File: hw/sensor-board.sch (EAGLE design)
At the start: 51 parts, among them U1 LT1762EMS8-3.3PBF, U2 ULN2003LVPWR, U3 ULN2003LVPWR, U4 PCA9685PW, U5 AT42QT1070-SSU, X1 MOLEX-501953-0407, X2 MOLEX-501953-0407

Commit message: Switched VDD of LED PWM driver to 3.3V.
Added an LDO to generate VDD for LED PWM driver.
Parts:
- added C5: 0.01uF 25V, rcl:C-EUC0603K
- added C6, C8: 1uF 25V, rcl:C-EUC0603K
- added U6: TPS730XX, vreg:TPS730XX
- renumbered 5V to 3.3V
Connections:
- new net N$1: C5.1, U6.NR
- new net N$9: 3.3V.TP, C6.2, TP1.TP, U4.A3, U4.VDD, U6.OUT
- net GND: now also C5.2, C6.1, C8.2, U2.IN7, U3.IN7, U6.GND
- net VDD_5: now also C8.1, U6.EN, U6.IN; no longer 3.3V.TP, TP1.TP, U4.A3, U4.VDD

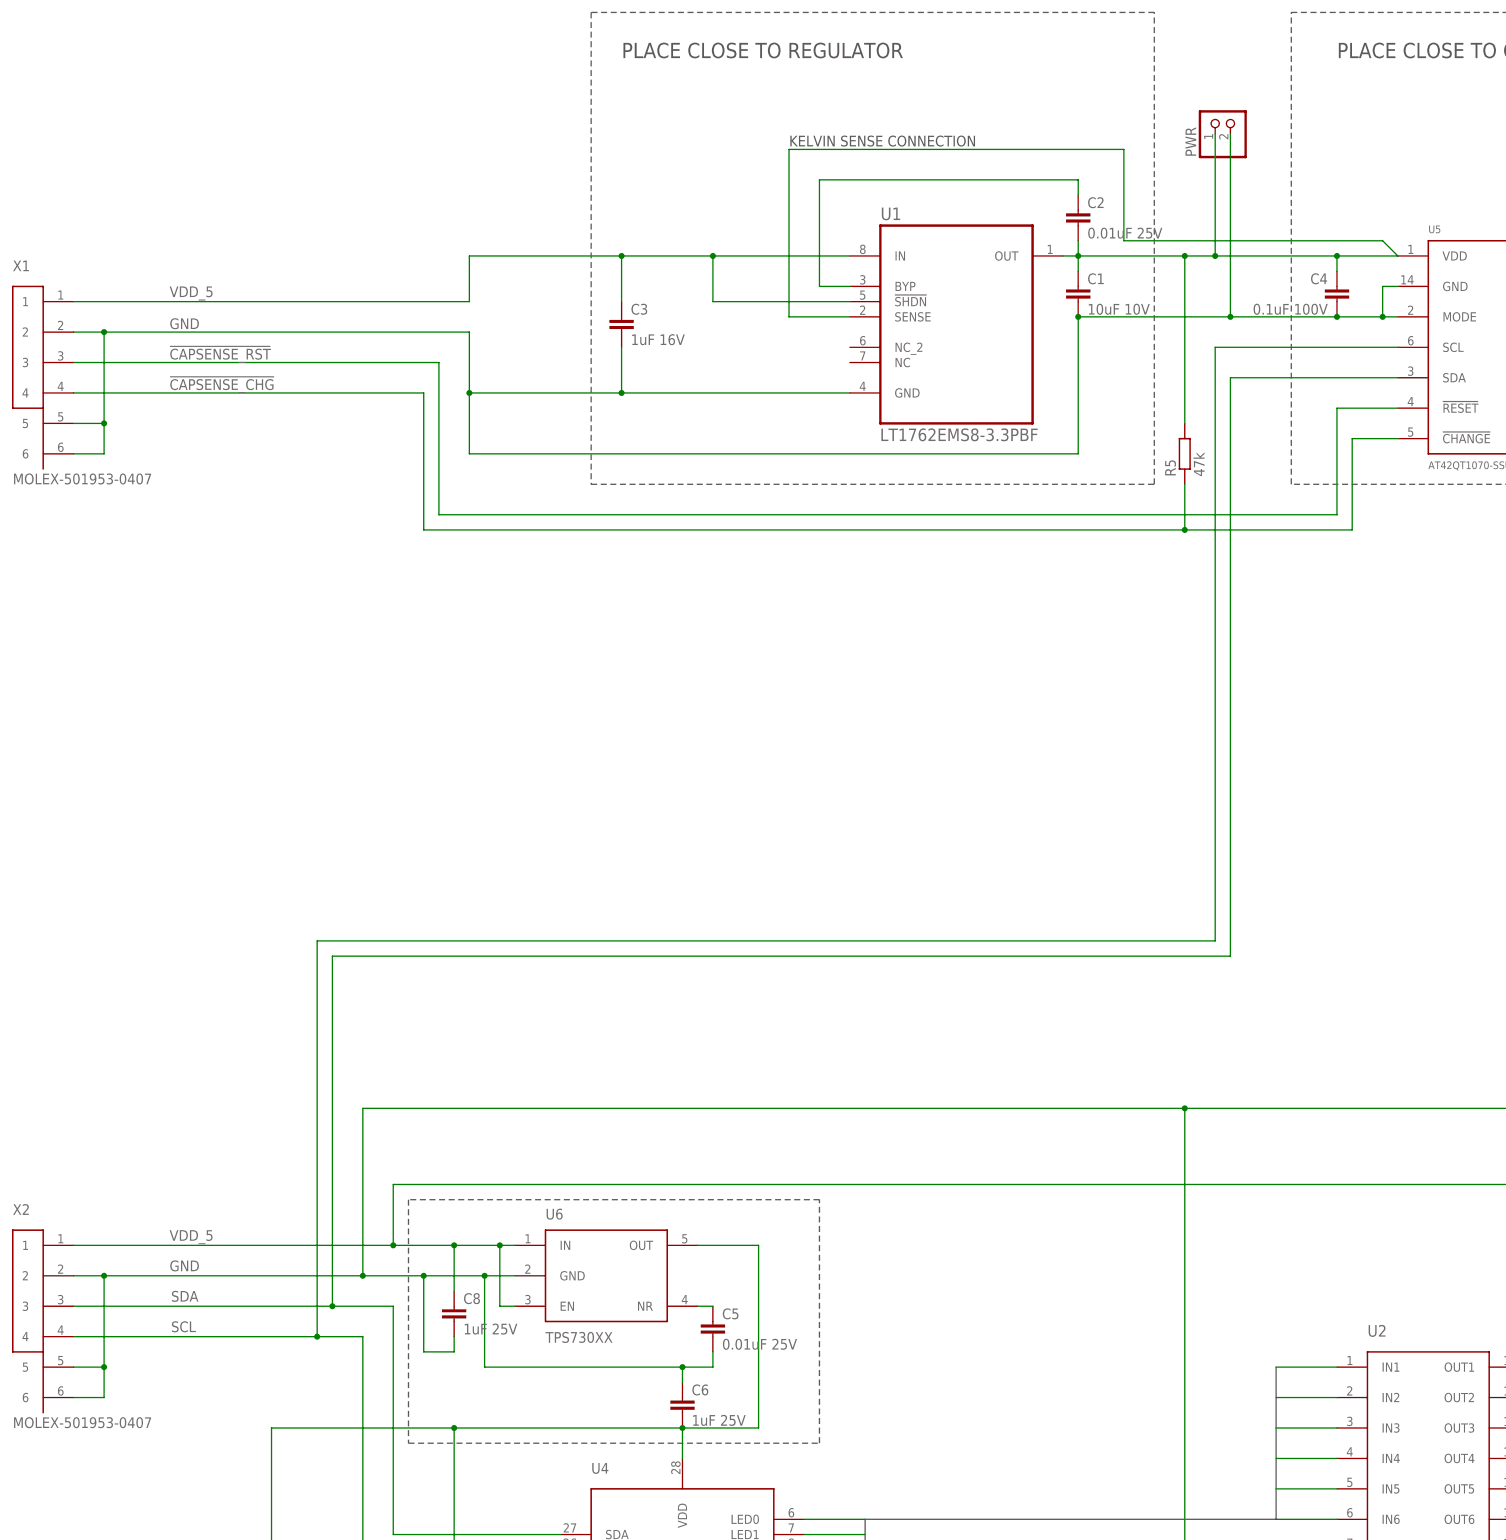
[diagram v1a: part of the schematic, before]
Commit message: Update part number and values for LDO caps.
Optimize cap placement near LDOs.
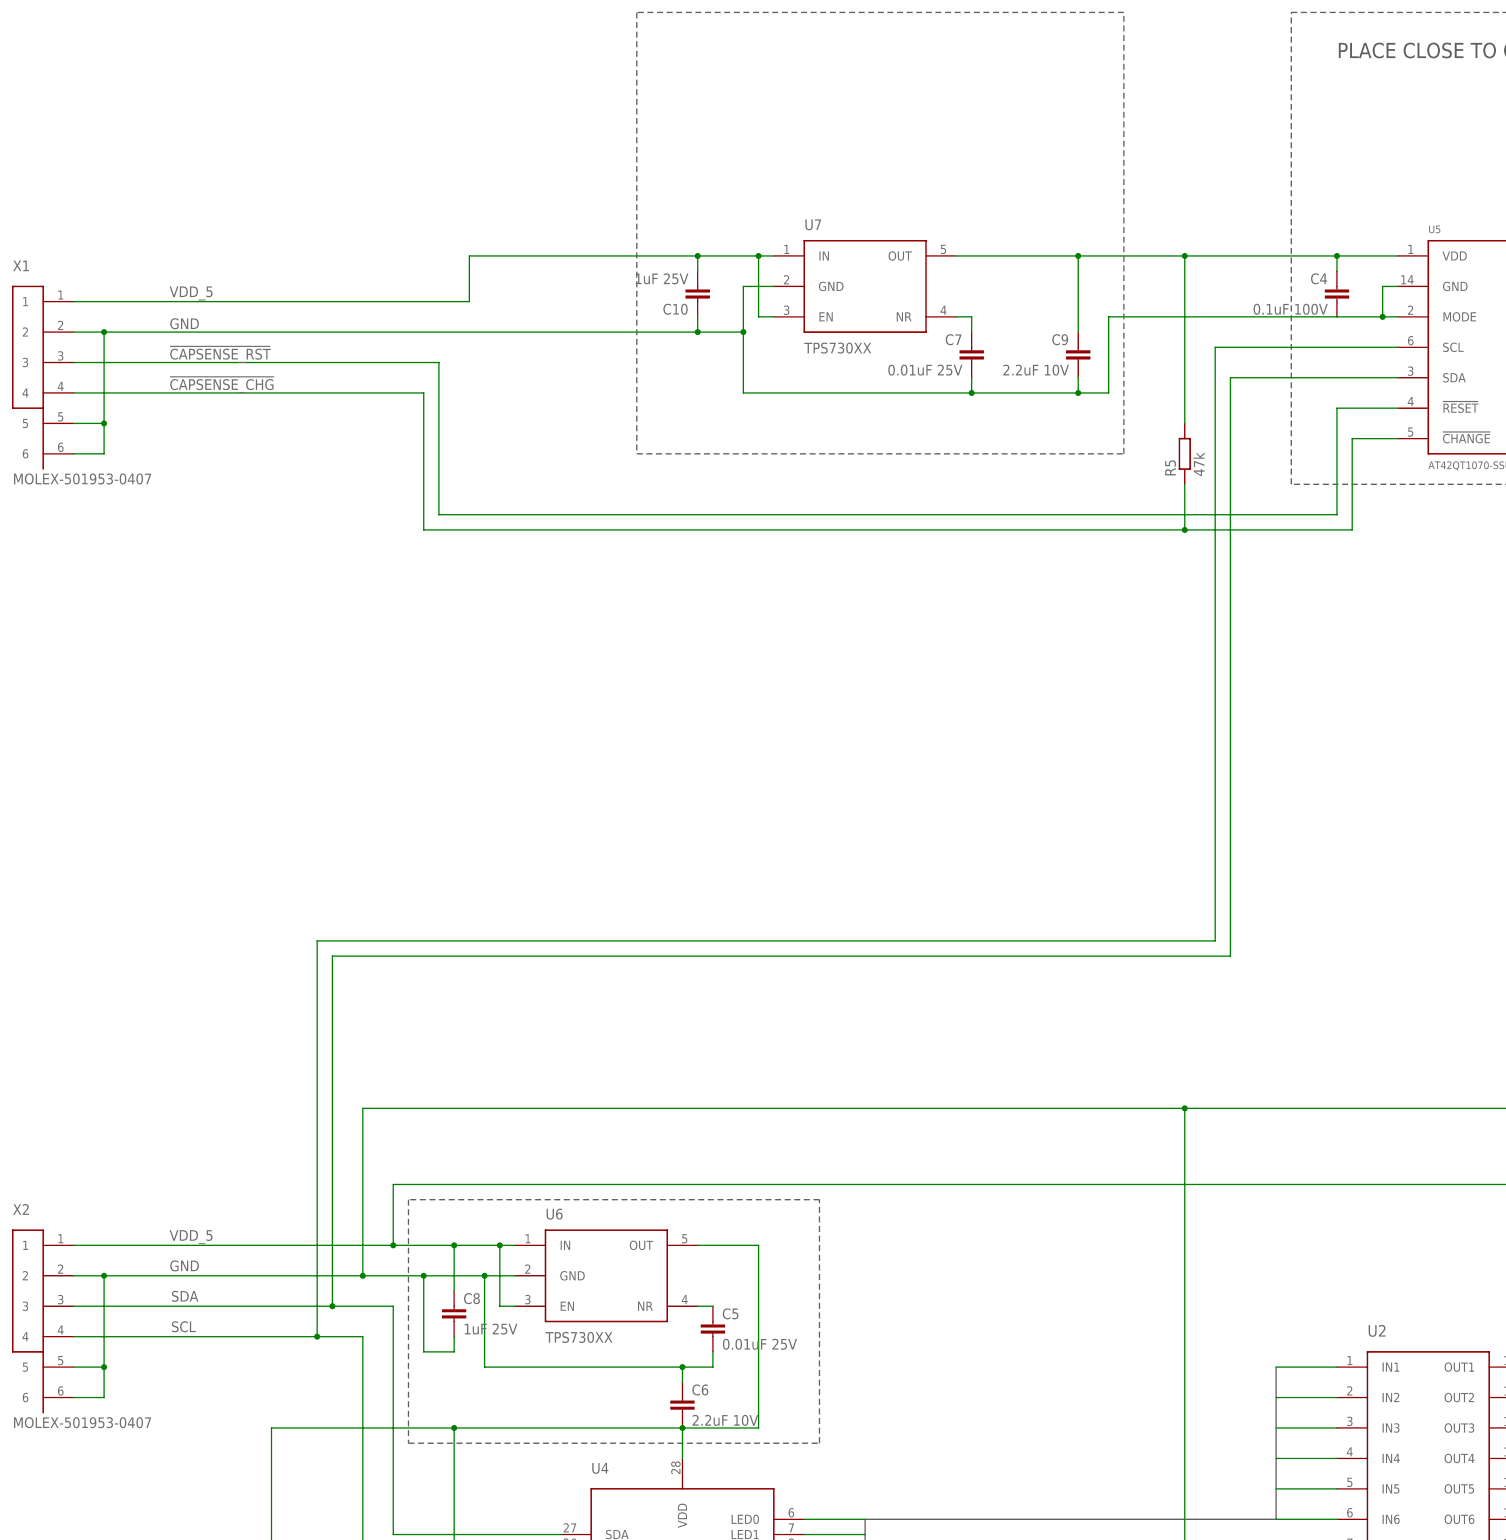
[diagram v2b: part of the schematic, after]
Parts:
- removed C1: 10uF 10V, rcl:C-EUC0805K
- removed C2: 0.01uF 25V, rcl:C-EUC0402K
- removed C3: 1uF 16V, rcl:C-EUC0603K
- removed PWR: (no value), pinhead:PINHD-1X2
- removed U1: LT1762EMS8-3.3PBF, vreg:LT1762EMS8-3.3PBF
- added C10: 1uF 25V, rcl:C-EUC0402K
- added C7: 0.01uF 25V, rcl:C-EUC0402K
- added C9: 2.2uF 10V, rcl:C-EUC0402K
- added U7: TPS730XX, vreg:TPS730XX
- C5: device rcl:C-EUC0603K -> rcl:C-EUC0402K
- C6: value 1uF 25V -> 2.2uF 10V; device rcl:C-EUC0603K -> rcl:C-EUC0402K; ELEMENT14_URL http://sg.element14.com/jsp/search/productdetail.jsp?sku=2146156 -> http://sg.element14.com/jsp/search/productdetail.jsp?sku=2118127; MFR_PART C1608X7R1C105K080AC -> C0402C225M8PAC TU
- C8: device rcl:C-EUC0603K -> rcl:C-EUC0402K; ELEMENT14_URL http://sg.element14.com/jsp/search/productdetail.jsp?sku=21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 -> http://sg.element14.com/jsp/search/productdetail.jsp?sku=18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; MFR_PART C1608X7R1C105K080AC -> C1005X5R1A105K050BB
- R5: device myrcl:R-EU_NKR0603 -> myrcl:R-EU_NKR0402; ELEMENT14_URL http://sg.element14.com/jsp/search/productdetail.jsp?sku=1799462 -> http://sg.element14.com/jsp/search/productdetail.jsp?sku=1799288; MFR_PART RC0603JR-1047KL -> RC0402JR-0747KL
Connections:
- net GND: now also C10.1, C7.2, C9.2, U7.GND; no longer C1.2, C3.2, PWR.2, U1.GND
- net N$8: now also C7.1, U7.NR; no longer C2.1, U1.BYP
- net VDD_3_3: now also C9.1, U7.OUT; no longer C1.1, C2.2, PWR.1, U1.OUT, U1.SENSE
- net VDD_5: now also C10.2, U7.EN, U7.IN; no longer C3.1, U1.!SHDN!, U1.IN
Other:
- note removed: "KELVIN SENSE CONNECTION"
- note removed: "PLACE CLOSE TO REGULATOR"

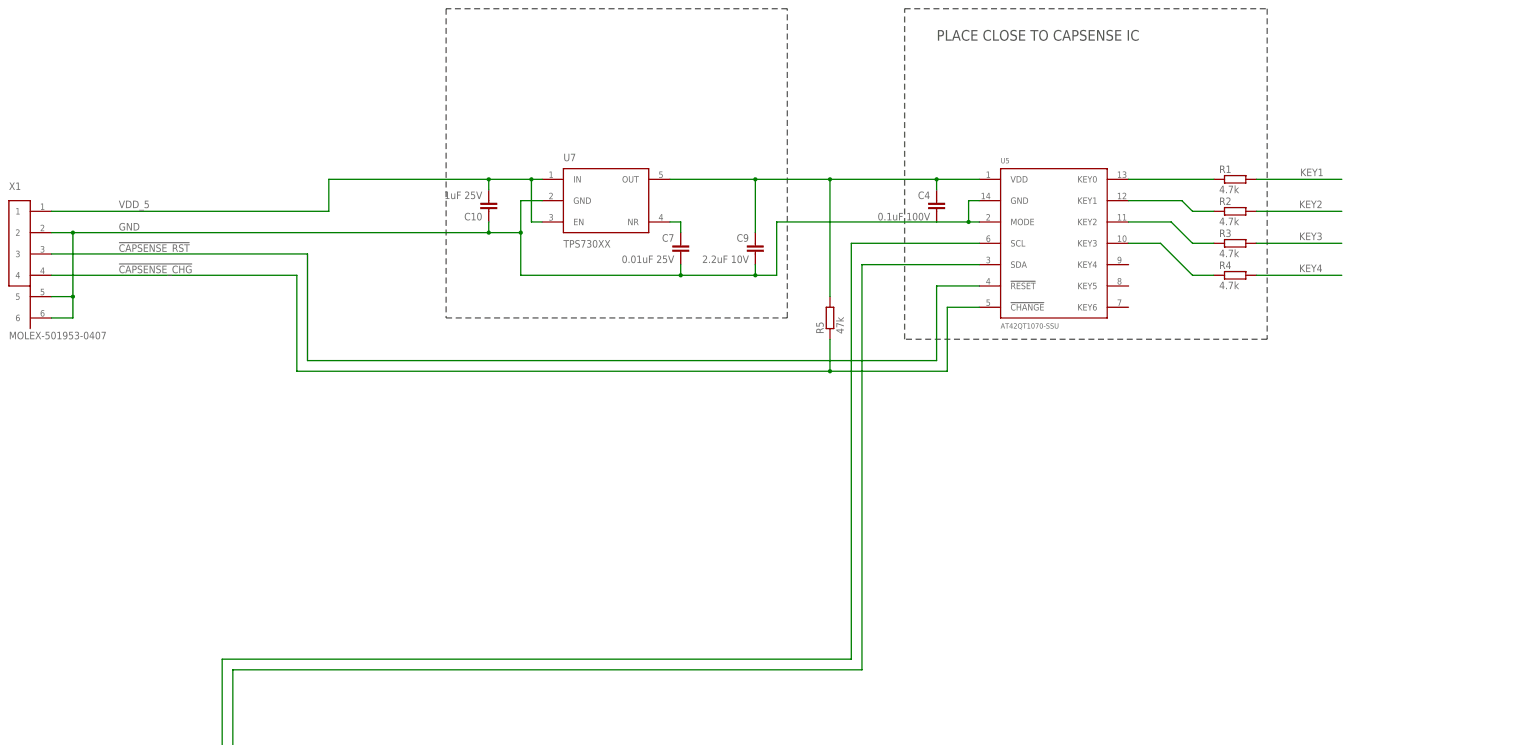
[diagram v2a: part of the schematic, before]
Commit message: Route unused sensing lines to test points.
Resolve DRC issues due to silkscreen over stop mask.
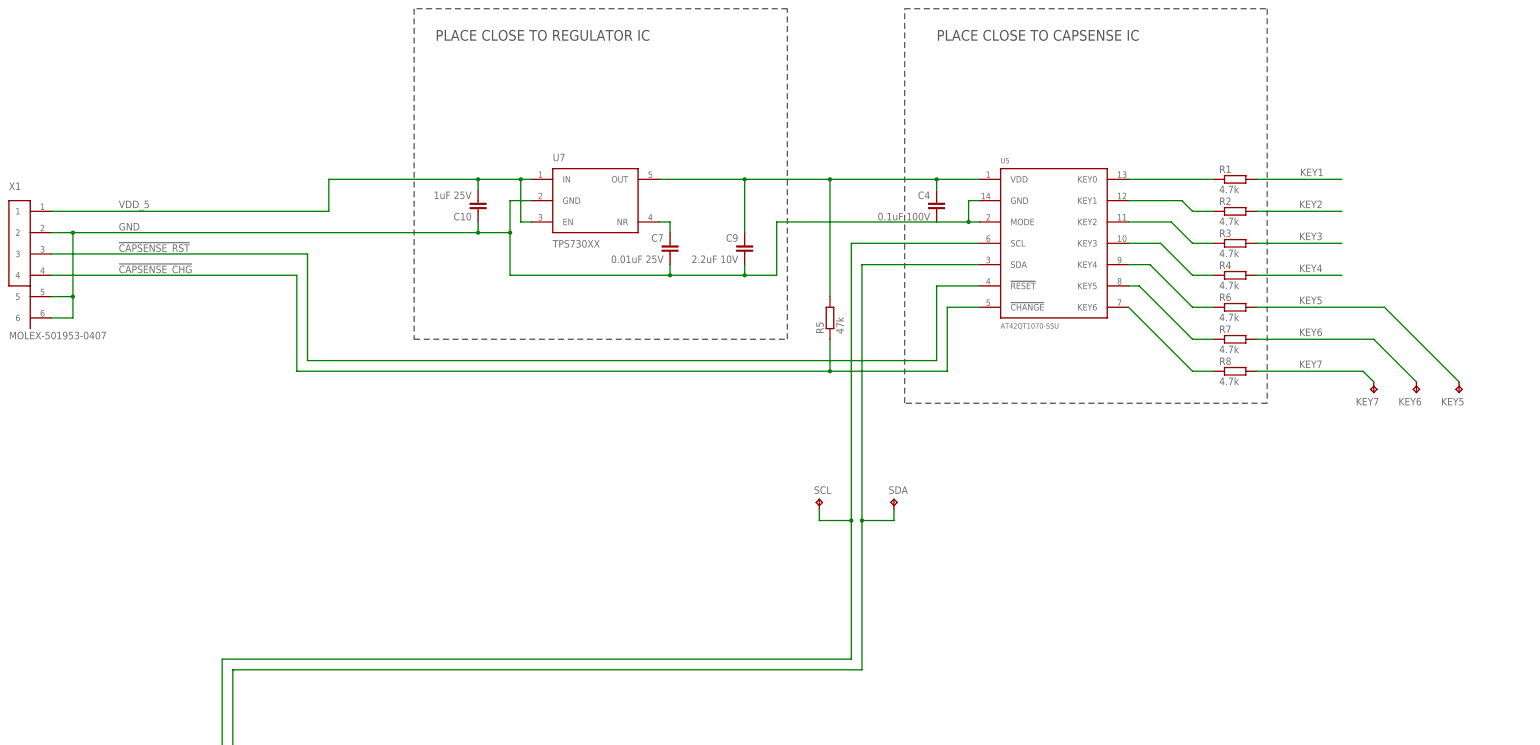
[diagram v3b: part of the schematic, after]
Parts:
- added KEY5, KEY6, KEY7, SCL, SDA: TPTP06R, testpad:TPTP06R
- added R6, R7, R8: 4.7k, myrcl:R-EU_NKR0402
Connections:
- new net KEY5: KEY5.TP, R6.2
- new net KEY6: KEY6.TP, R7.2
- new net KEY7: KEY7.TP, R8.2
- new net N$10: R6.1, U5.KEY4
- new net N$11: R7.1, U5.KEY5
- new net N$12: R8.1, U5.KEY6
- net SCL: now also SCL.TP
- net SDA: now also SDA.TP
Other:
- note added: "PLACE CLOSE TO REGULATOR IC"
- moved on the sheet: C10, C7, C9, U7

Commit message: Sync part names for LED caps and resistors.
Label power supply nets.
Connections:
- net N$9 renamed VDD_3_3_PWMDRIVE
- net VDD_3_3 renamed VDD_3_3_CAPSENSE
- removed net VDD_5: C10.2, C13.2, C14.2, C15.2, C16.2, C17.2, C18.2, C19.2, C20.2, C21.2, C22.2, C23.2, C24.2, C8.1, D1.4-AR, D1.5-AG, D1.6-AB, D2.4-AR, D2.5-AG, D2.6-AB, D3.4-AR, D3.5-AG, D3.6-AB, D4.4-AR, D4.5-AG, D4.6-AB, U2.COM, U3.COM, U6.EN, U6.IN, U7.EN, U7.IN, X1.1, X2.1
- new net VDD_5_CAPSENSE: C10.2, U7.EN, U7.IN, X1.1
- new net VDD_5_ILLUM: C13.2, C14.2, C15.2, C16.2, C17.2, C18.2, C19.2, C20.2, C21.2, C22.2, C23.2, C24.2, C8.1, D1.4-AR, D1.5-AG, D1.6-AB, D2.4-AR, D2.5-AG, D2.6-AB, D3.4-AR, D3.5-AG, D3.6-AB, D4.4-AR, D4.5-AG, D4.6-AB, U2.COM, U3.COM, U6.EN, U6.IN, X2.1
